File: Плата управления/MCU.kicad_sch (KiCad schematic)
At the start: 19 parts, among them U7 ASEMB-10, U8 STM32F407VETx

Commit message: Редактировал схему
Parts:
- added R29 (x2): 1k, Resistor_SMD:R_0603_1608Metric_Pad0.98x0.95mm_HandSolder, symbol Device:R_Small
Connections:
- net +3.3V: now also R29.1
- net CAN1_RXD_MCU: now also U8.70 (PA11); no longer U8.51 (PB12)
- net CAN1_TXD_MCU: now also U8.71 (PA12); no longer U8.52 (PB13)
- net CAN2_RXD_MCU: now also U8.51 (PB12); no longer U8.70 (PA11)
- net CAN2_TXD_MCU: now also U8.52 (PB13); no longer U8.71 (PA12)
- net GND: now also R29.1
- net NRST: now reaches U8.14 (NRST)
- net NRST: now also R29.2
- net Angle_Sensor_CS_MCU: now reaches U8.77 (PA15)
- net Angle_Sensor_SCLK_MCU: now reaches U8.78 (PC10)
- net Angle_Sensor_SDIO_MCU: now reaches U8.79 (PC11)
- net BOOT0: now reaches U8.94 (BOOT0)
- net BOOT0: now also R29.2
- net MISO_MCU renamed EEPROM_MISO_MCU
- net MOSI_MCU renamed EEPROM_MOSI_MCU
- net RX_MCU renamed RS_485_TX_MCU
- net SCK_MCU renamed EEPROM_SCK_MCU
- net SCL_MCU renamed Temperature_Power_SCL_MCU
- net SDA_MCU renamed Temperature_Power_SDA_MCU
- net TX_MCU renamed RS_485_RX_MCU
- net ~{CS_MCU} renamed EEPROM_~{CS_MCU}
- net ~{OS}_MCU renamed Temperature_Power_~{OS}_MCU
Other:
- note added: "Питание МК"
- moved on the sheet: C24, C32, FB1, R24

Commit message: Ещё нужно доработать
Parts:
- added C13, C17: 1u, Capacitor_SMD:C_0603_1608Metric_Pad1.08x0.95mm_HandSolder, symbol Device:C_Small
- added C16: 100n, Capacitor_SMD:C_0603_1608Metric_Pad1.08x0.95mm_HandSolder, symbol Device:C_Small
- added C5, C6: 2.2u, Capacitor_SMD:C_0603_1608Metric_Pad1.08x0.95mm_HandSolder, symbol Device:C_Small
- added R29 (x3): 0, Resistor_SMD:R_0603_1608Metric_Pad0.98x0.95mm_HandSolder, symbol Device:R_Small
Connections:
- net +3.3VA: now also C13.1, C16.1, C17.1
- net Angle_Sensor_SDIO_MCU: now also R29.2, R29.2; no longer U8.79 (PC11)
- net GND: now also C5.2, C6.2, R29.2; no longer U8.13 (PH1)
- net GNDA: now also C13.2, C16.2, C17.2
- net OUT_MCU: now reaches U8.33 (PC4)
- net at U8.49 (VCAP_1): now also C6.1
- net at U8.73 (VCAP_2): now also C5.1
- net at U8.80 (PC12): now also R29.1
- new net: R29.1, U8.13 (PH1)
- new net: R29.1, U8.79 (PC11)
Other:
- moved on the sheet: C21, C22, C23, C26, C27, C28, C29, C30, C31, C33, C34, C35

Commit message: Собираю документацию
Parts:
- added C46, C47: 1u, Capacitor_SMD:C_0603_1608Metric_Pad1.08x0.95mm_HandSolder, symbol Device:C_Small
- added D12, D13: BAT54S, Package_TO_SOT_SMD:SOT-23, symbol Diode:BAT54S
- added R29 (x2): 0, Resistor_SMD:R_0603_1608Metric_Pad0.98x0.95mm_HandSolder, symbol Device:R_Small
- added R30 (x4): 120, Resistor_SMD:R_0603_1608Metric_Pad0.98x0.95mm_HandSolder, symbol Device:R_Small
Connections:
- net +3.3VA: now also D12.2 (K), D13.2 (K)
- net Analog_Input1: now also R30.1; no longer U8.35 (PB0)
- net Analog_Input2: now also R30.1; no longer U8.36 (PB1)
- net GNDA: now also C46.1, C47.1, D12.1 (A), D13.1 (A), R30.1, R30.1
- net OUT_MCU: now also R29.2, R29.2; no longer U8.33 (PC4)
- net at R29.1, U8.80 (PC12): now also R29.1
- net SWDIO: now reaches U8.72 (PA13)
- net SWCLK: now reaches U8.76 (PA14)
- new net: C46.2, D12.3 (COM), R30.2, R30.2, U8.35 (PB0)
- new net: C47.2, D13.3 (COM), R30.2, R30.2, U8.36 (PB1)
- new net: R29.1, U8.33 (PC4)

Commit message: Добавил документы
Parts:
- removed C47: 1u, Capacitor_SMD:C_0603_1608Metric_Pad1.08x0.95mm_HandSolder, symbol Device:C_Small
- removed D13: BAT54S, Package_TO_SOT_SMD:SOT-23, symbol Diode:BAT54S
- removed R30 (x2): 120, Resistor_SMD:R_0603_1608Metric_Pad0.98x0.95mm_HandSolder, symbol Device:R_Small
- added D15: BAT54S, Package_TO_SOT_SMD:SOT-23, symbol Diode:BAT54S
- added R30: 0, Resistor_SMD:R_0603_1608Metric_Pad0.98x0.95mm_HandSolder, symbol Device:R_Small
- R30: value 120 -> 1.5k
- R30: value 120 -> 1k
- U8: value STM32F407VETx -> APM32F405xG
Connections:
- net +3.3V: now also D15.2 (K)
- net Digital_input1: now also R30.2; no longer U8.57 (PD10)
- net GND: now also D15.1 (A)
- net Digital_input2: no longer names the net of U8.56 (PD9)
- new net: D15.3 (COM), R30.1, U8.57 (PD10)
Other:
- moved on the sheet: C13, C16, C17, C19, C21, C22, C23, C24, C26, C27, C28, C29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

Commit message: Добавил все документы
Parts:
- renumbered C24 to C11, C32 to C12, C16 to C14, C17 to C15, C19 to C16, C21 to C17, C26 to C18, C29 to C19, C33 to C20, C22 to C21, C27 to C22, C30 to C23, C34 to C24, C46 to C25, C23 to C26, C28 to C27, C31 to C28, C35 to C29, C6 to C30, C5 to C31, D12 to D4, D15 to D5, R24 to R20, U7 to U6, U8 to U7

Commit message: Версия под отчёт
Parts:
- added C55: 1u, Capacitor_SMD:C_0603_1608Metric_Pad1.08x0.95mm_HandSolder, symbol Device:C_Small
- added D14, D15: BAT54S, Package_TO_SOT_SMD:SOT-23, symbol Diode:BAT54S
- added R30: 1k, Resistor_SMD:R_0603_1608Metric_Pad0.98x0.95mm_HandSolder, symbol Device:R_Small
- added R30: 1.5k, Resistor_SMD:R_0603_1608Metric_Pad0.98x0.95mm_HandSolder, symbol Device:R_Small
- added R30: 0, Resistor_SMD:R_0603_1608Metric_Pad0.98x0.95mm_HandSolder, symbol Device:R_Small
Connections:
- net +3.3V: now also D15.2 (K)
- net +3.3VA: now also D14.2 (K)
- net GND: now also D15.1 (A)
- net GNDA: now also C55.1, D14.1 (A), R30.1
- net at U7.36 (PB1): now also C55.2, D14.3 (COM), R30.2, R30.2
- net at U7.56 (PD9): now also D15.3 (COM), R30.1
- new net Analog_Input2: R30.1
- new net Digital_input2: R30.2

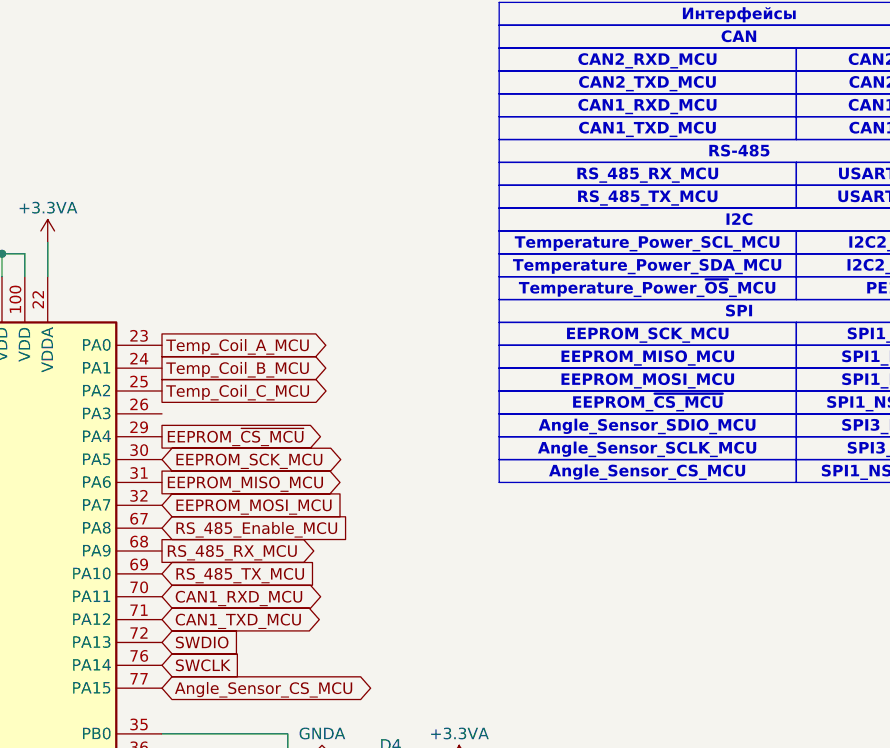
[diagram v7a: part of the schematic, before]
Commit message: Исправил RX и TX у шины RS485 и разъединил ножки управления шиной
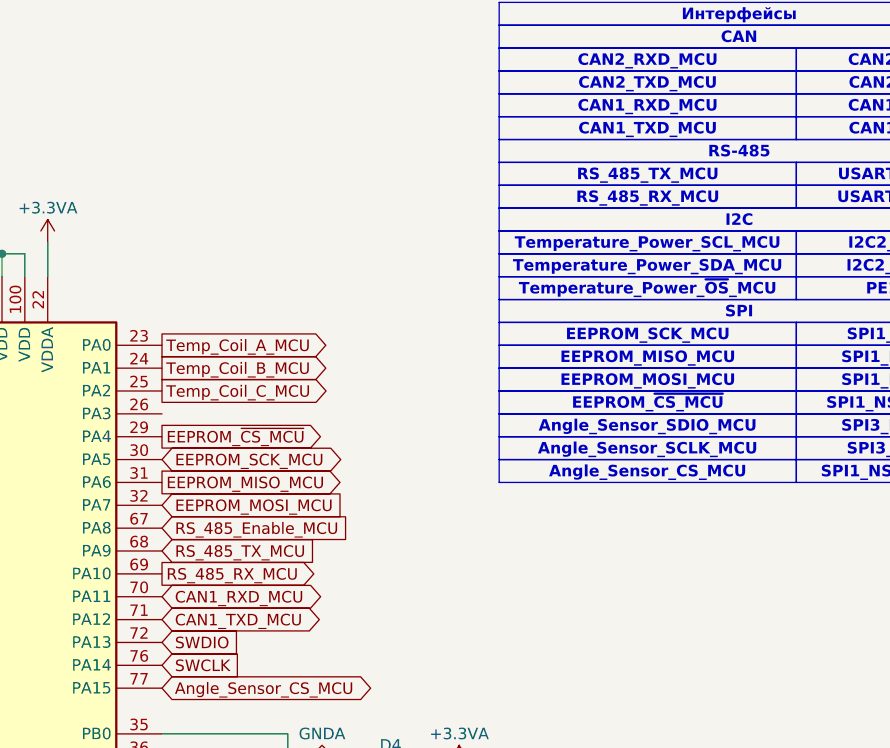
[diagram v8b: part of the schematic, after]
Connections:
- net RS_485_RX_MCU: now also U7.69 (PA10); no longer U7.68 (PA9)
- net RS_485_TX_MCU: now also U7.68 (PA9); no longer U7.69 (PA10)
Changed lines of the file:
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@@
   )
   (text_box "RS_485_RX_MCU"
-    (at 144.145 27.305 0) (size 33.02 2.54)
+    (at 144.145 29.845 0) (size 33.02 2.54)
     (stroke (width 0) (type default))
     (fill (type none))
@@
   )
   (text_box "RS_485_TX_MCU"
-    (at 144.145 29.845 0) (size 33.02 2.54)
+    (at 144.145 27.305 0) (size 33.02 2.54)
     (stroke (width 0) (type default))
     (fill (type none))
@@
     )
   )
-  (global_label "RS_485_RX_MCU" (shape output) (at 106.68 70.485 0) (fields_autoplaced)
-    (effects (font (size 1.27 1.27)) (justify left))
-    (property "Intersheetrefs" "${INTERSHEET_REFS}" (at 125.2074 70.485 0)
+  (global_label "RS_485_RX_MCU" (shape output) (at 106.68 73.025 0) (fields_autoplaced)
+    (effects (font (size 1.27 1.27)) (justify left))
+    (property "Intersheetrefs" "${INTERSHEET_REFS}" (at 125.2074 73.025 0)
       (effects (font (size 1.27 1.27)) (justify left) hide)
     )
@@
     )
   )
-  (global_label "RS_485_TX_MCU" (shape input) (at 106.68 73.025 0) (fields_autoplaced)
-    (effects (font (size 1.27 1.27)) (justify left))
-    (property "Intersheetrefs" "${INTERSHEET_REFS}" (at 124.905 73.025 0)
-      (effects (font (size 1.27 1.27)) (justify left) hide)
-    )
+  (global_label "RS_485_TX_MCU" (shape input) (at 106.68 70.485 0) (fields_autoplaced)
+    (effects (font (size 1.27 1.27)) (justify left))
+    (property "Intersheetrefs" "${INTERSHEET_REFS}" (at 124.905 70.485 0)
+      (effects (font (size 1.27 1.27)) (justify left) hide)
+    )
